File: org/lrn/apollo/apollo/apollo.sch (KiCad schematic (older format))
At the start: 53 parts, among them J1 Conn_01x01_Male, J10 Conn_01x01_Male, J11 Conn_01x01_Male, J2 Conn_01x01_Male, J3 Conn_01x01_Male, J4 Conn_01x01_Male, J5 Conn_01x01_Male, J6 Conn_01x01_Male, J7 Conn_01x01_Male, J8 Conn_01x01_Male, J9 Conn_01x01_Male, K1 SRD-05VDC-SL-C, Q1 PN2222A, Q2 PN2222A, Q3 PN2222A, Q4 PN2222A, Q5 PN2222A, U1 74HC595, U2 5461AS-1, U3 74HC595, U4 ATmega168P-20PU

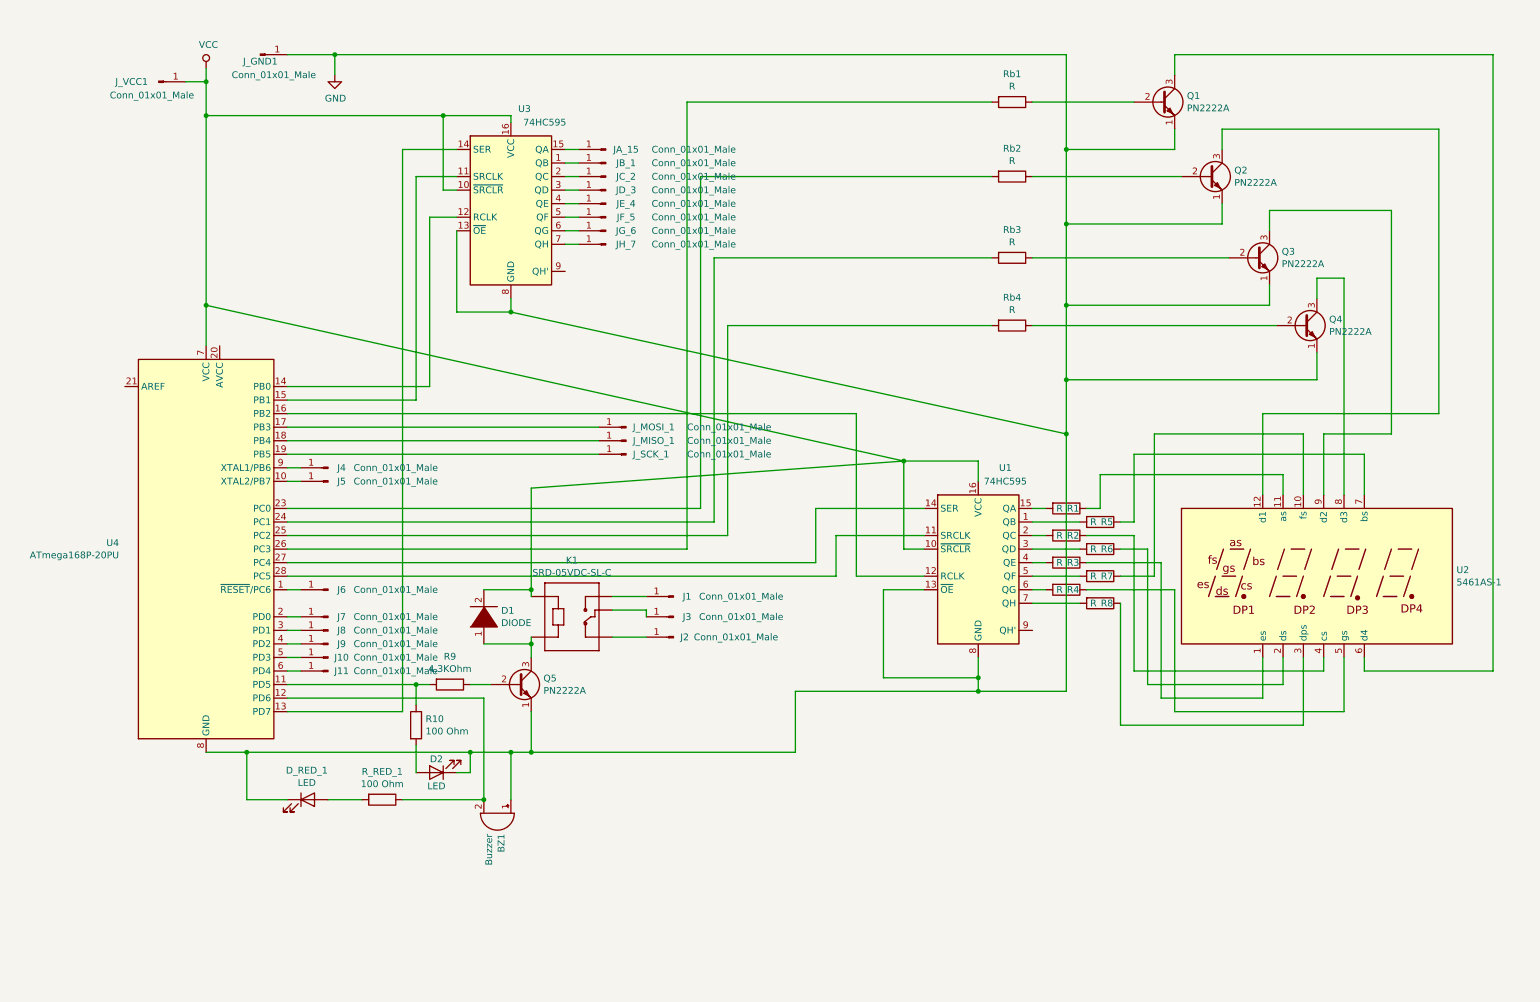
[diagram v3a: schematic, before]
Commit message: apollo: pcb improvements - separate two part of functuionality: display and control
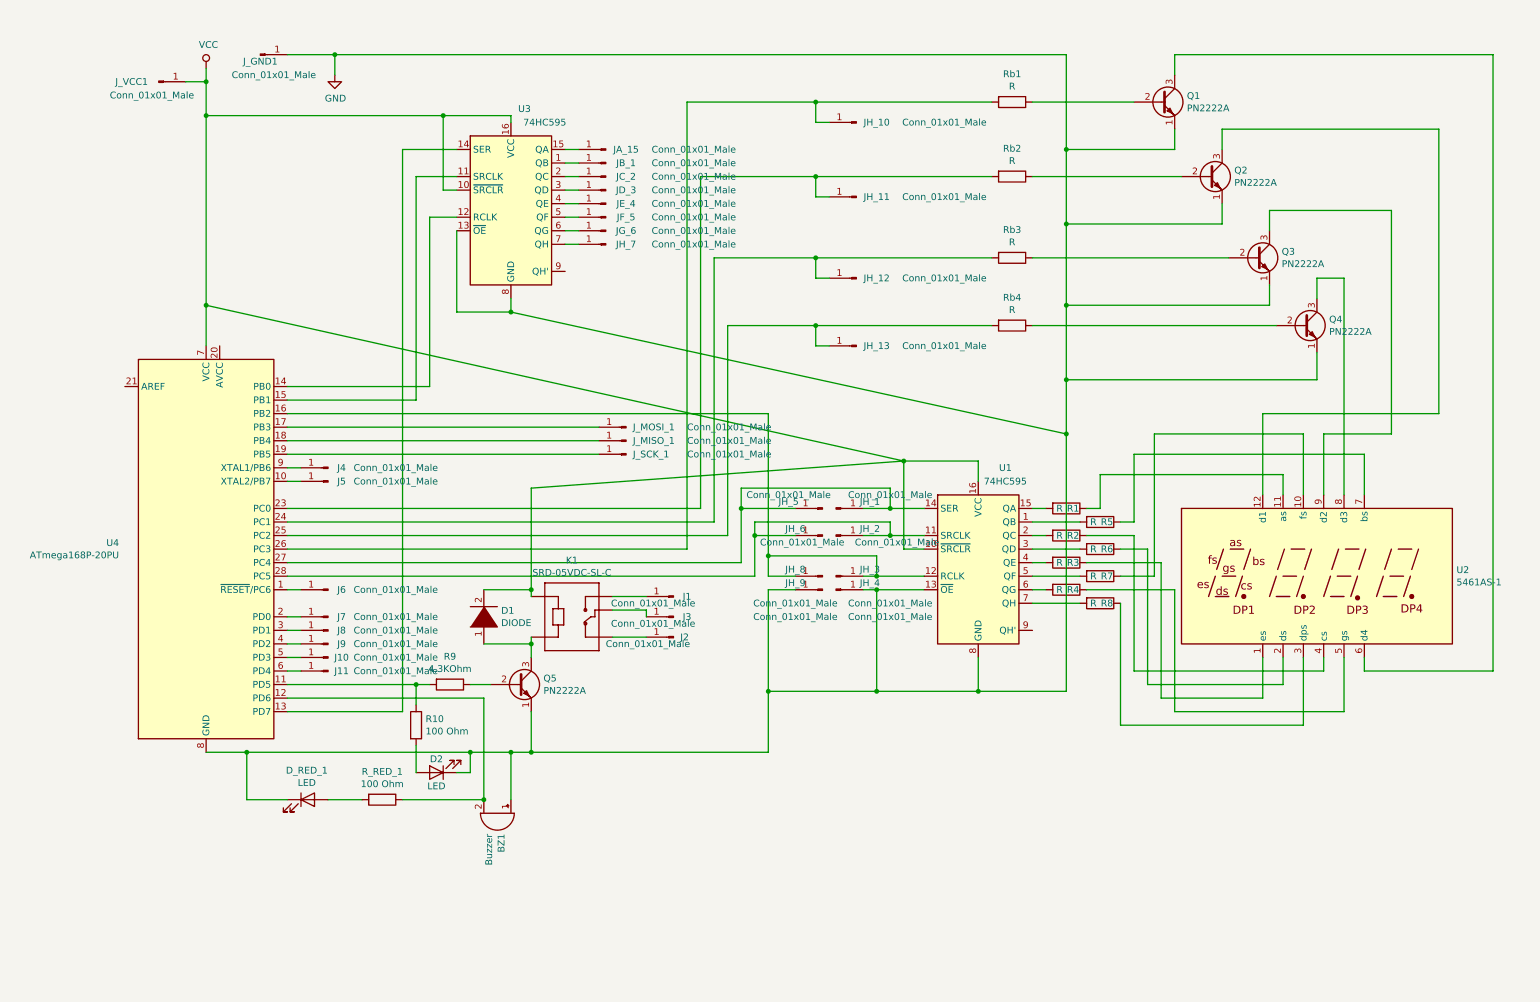
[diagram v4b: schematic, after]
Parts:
- added JH_1, JH_10, JH_11, JH_12, JH_13, JH_2, JH_3, JH_4, JH_5, JH_6, JH_8, JH_9: Conn_01x01_Male, Connector_Pin:Pin_D0.7mm_L6.5mm_W1.8mm_FlatFork, symbol Connector:Conn_01x01_Male
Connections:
- net GND: now also JH_4.1 (Pin_1), JH_9.1 (Pin_1)
- net at U1.11 (SRCLK), U4.28 (PC5): now also JH_2.1 (Pin_1), JH_6.1 (Pin_1)
- net at U1.12 (RCLK), U4.16 (PB2): now also JH_3.1 (Pin_1), JH_8.1 (Pin_1)
- net at U1.14 (SER), U4.27 (PC4): now also JH_1.1 (Pin_1), JH_5.1 (Pin_1)
- net at Rb1.2, U4.26 (PC3): now also JH_10.1 (Pin_1)
- net at Rb2.2, U4.23 (PC0): now also JH_11.1 (Pin_1)
- net at Rb3.2, U4.24 (PC1): now also JH_12.1 (Pin_1)
- net at Rb4.2, U4.25 (PC2): now also JH_13.1 (Pin_1)

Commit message: apollo: global refactoring for schematic and add relay_2
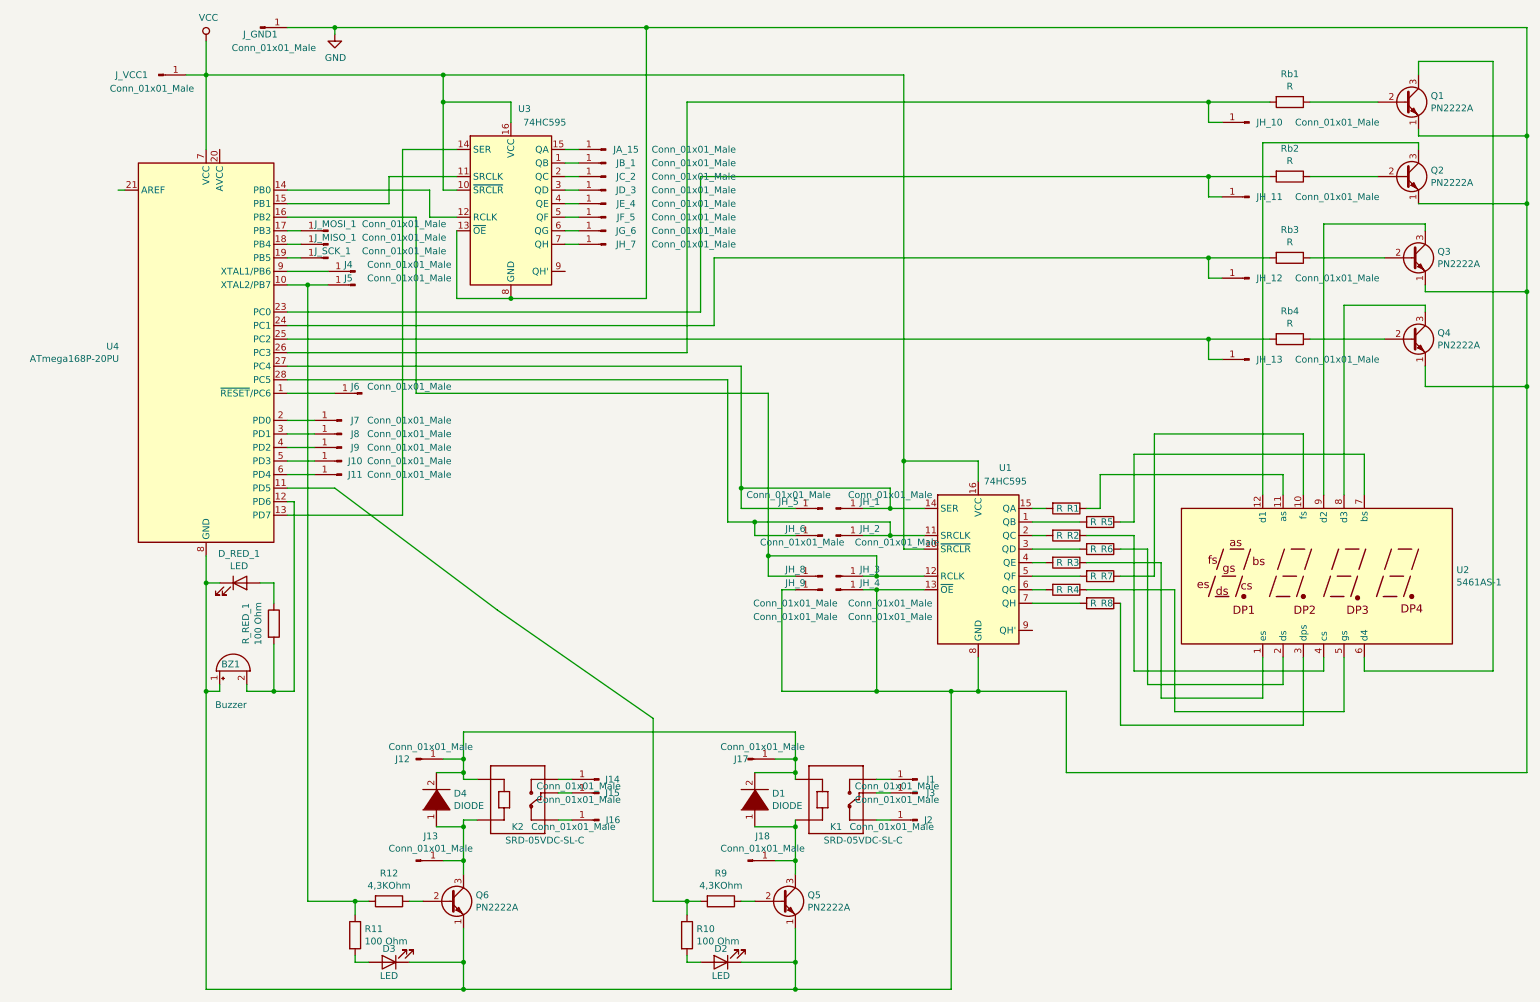
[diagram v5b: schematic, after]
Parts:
- added D3: LED, LED_THT:LED_D5.0mm_FlatTop, symbol Device:LED
- added D4: DIODE, apollo:D__Horizontal, symbol pspice:DIODE
- added J12, J13, J14, J15, J16, J17, J18: Conn_01x01_Male, Connector_Pin:Pin_D0.7mm_L6.5mm_W1.8mm_FlatFork, symbol Connector:Conn_01x01_Male
- added K2: SRD-05VDC-SL-C, apollo:RELAY_SRD-05VDC-SL-C, symbol SRD-05VDC-SL-C:SRD-05VDC-SL-C
- added Q6: PN2222A, apollo:2N222A-TO-92_Wide, symbol Transistor_BJT:PN2222A
- added R11: 100 Ohm, apollo:R__Horizontal, symbol Device:R
- added R12: 4,3KOhm, apollo:R__Horizontal, symbol Device:R
- D1: footprint apollo:R__Horizontal -> apollo:D__Horizontal
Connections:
- net GND: now also D3.1 (K), Q6.1 (E)
- net VCC: no longer D1.2 (A), K1.A1
- net at J5.1 (Pin_1), U4.10 (XTAL2/PB7): now also R11.1, R12.2
- net at BZ1.2 (+), U4.12 (PD6): now also R_RED_1.2; no longer R_RED_1.1
- net at D_RED_1.2 (A): now also R_RED_1.1; no longer R_RED_1.2
- net at D1.1 (K), K1.A2, Q5.3 (C): now also J18.1 (Pin_1)
- new net: D1.2 (A), D4.2 (A), J12.1 (Pin_1), J17.1 (Pin_1), K1.A1, K2.A1
- new net: Q6.2 (B), R12.1
- new net: D4.1 (K), J13.1 (Pin_1), K2.A2, Q6.3 (C)
- new net: J15.1 (Pin_1), K2.COM
- new net: J16.1 (Pin_1), K2.NC
- new net: J14.1 (Pin_1), K2.NO
- new net: D3.2 (A), R11.2
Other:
- moved on the sheet: BZ1, D1, D2, D_RED_1, J1, J10, J11, J2, J3, J4, J5, J6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

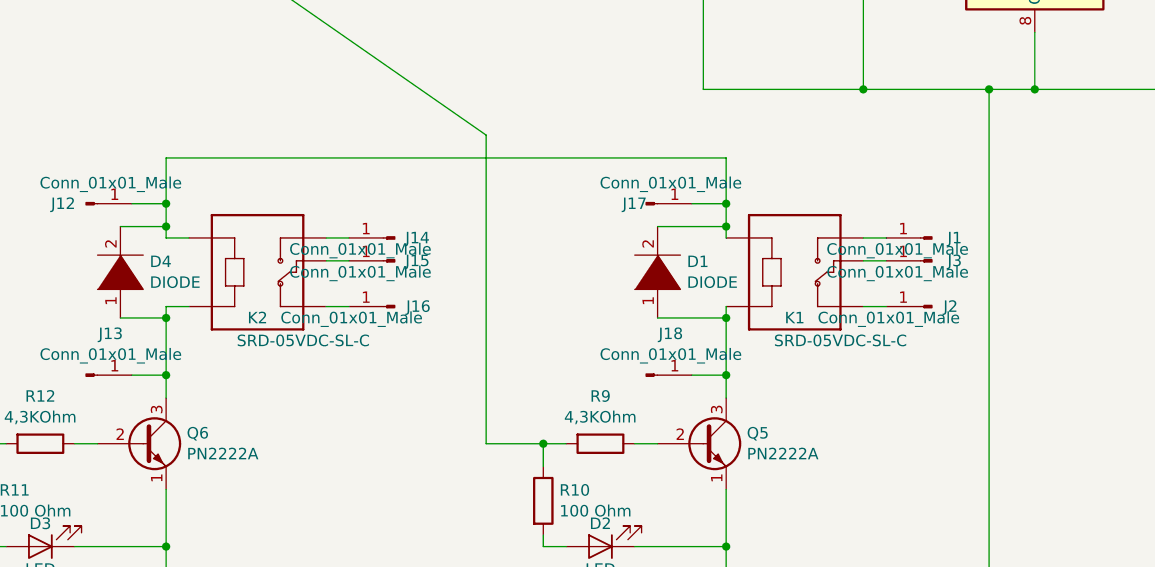
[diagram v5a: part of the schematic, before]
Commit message: apollo: remove relays (connectors instead)
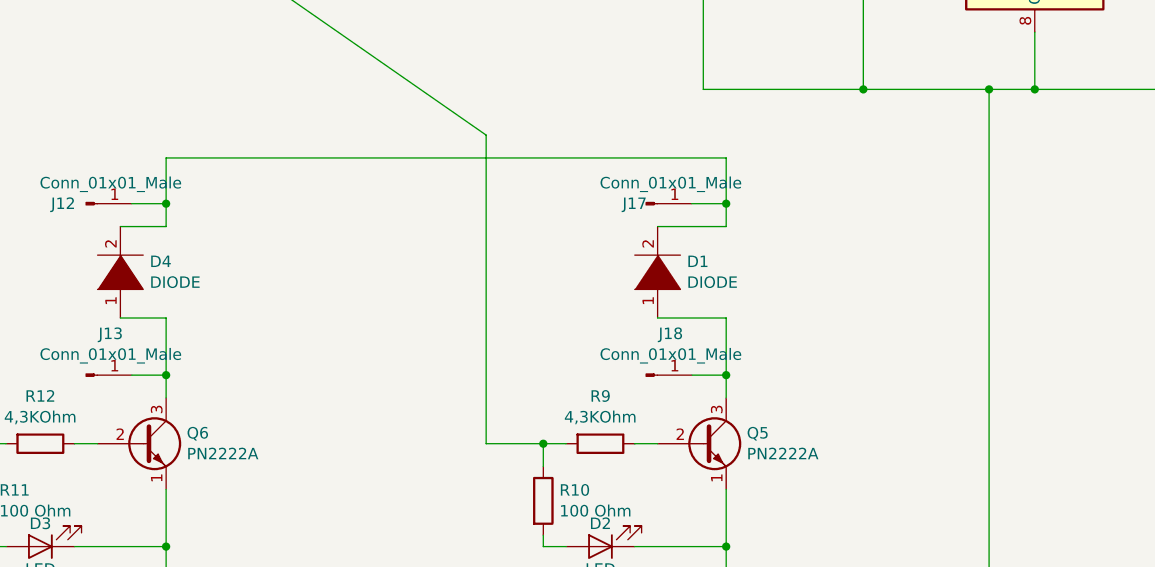
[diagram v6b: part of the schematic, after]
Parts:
- removed J1, J14, J15, J16, J2, J3: Conn_01x01_Male, Connector_Pin:Pin_D0.7mm_L6.5mm_W1.8mm_FlatFork, symbol Connector:Conn_01x01_Male
- removed K1, K2: SRD-05VDC-SL-C, apollo:RELAY_SRD-05VDC-SL-C, symbol SRD-05VDC-SL-C:SRD-05VDC-SL-C
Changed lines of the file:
@@
-$EndComp
-$Comp
-L SRD-05VDC-SL-C:SRD-05VDC-SL-C K1
-U 1 1 5F789B70
-P 6000 6250
-F 0 "K1" H 6000 6000 50  0000 C CNN
-F 1 "SRD-05VDC-SL-C" H 6200 5900 50  0000 C CNN
-F 2 "apollo:RELAY_SRD-05VDC-SL-C" H 6000 6250 50  0001 L BNN
-F 3 "IPC-7251" H 6000 6250 50  0001 L BNN
-F 4 "SONGLE RELAY" H 6000 6250 50  0001 L BNN "Field4"
-	1    6000 6250
-	1    0    0    -1
 $EndComp
 $Comp
@@
 $EndComp
 $Comp
-L Connector:Conn_01x01_Male J2
-U 1 1 5F7F3157
-P 6600 6450
-F 0 "J2" H 6550 6450 50  0000 R CNN
-F 1 "Conn_01x01_Male" H 7100 6500 50  0000 R CNN
-F 2 "Connector_Pin:Pin_D0.7mm_L6.5mm_W1.8mm_FlatFork" H 6600 6450 50  0001 C CNN
-F 3 "~" H 6600 6450 50  0001 C CNN
-	1    6600 6450
-	-1   0    0    1
-$EndComp
-$Comp
-L Connector:Conn_01x01_Male J1
-U 1 1 5F7F3A36
-P 6600 6150
-F 0 "J1" H 6500 6150 50  0000 C CNN
-F 1 "Conn_01x01_Male" H 6750 6200 50  0000 C CNN
-F 2 "Connector_Pin:Pin_D0.7mm_L6.5mm_W1.8mm_FlatFork" H 6600 6150 50  0001 C CNN
-F 3 "~" H 6600 6150 50  0001 C CNN
-	1    6600 6150
-	-1   0    0    1
-$EndComp
-$Comp
 L Device:R R10
 U 1 1 5F73C2C8
@@
 F 3 "~" H 5150 7500 50  0001 C CNN
 	1    5150 7500
-	-1   0    0    1
-$EndComp
-$Comp
-L Connector:Conn_01x01_Male J3
-U 1 1 5F74C3F1
-P 6600 6250
-F 0 "J3" H 6500 6250 50  0000 C CNN
-F 1 "Conn_01x01_Male" H 6750 6300 50  0000 C CNN
-F 2 "Connector_Pin:Pin_D0.7mm_L6.5mm_W1.8mm_FlatFork" H 6600 6250 50  0001 C CNN
-F 3 "~" H 6600 6250 50  0001 C CNN
-	1    6600 6250
 	-1   0    0    1
 $EndComp
@@
 $EndComp
 $Comp
-L Connector:Conn_01x01_Male J16
-U 1 1 5F8BDA7E
-P 4250 6450
-F 0 "J16" H 4200 6450 50  0000 R CNN
-F 1 "Conn_01x01_Male" H 4750 6500 50  0000 R CNN
-F 2 "Connector_Pin:Pin_D0.7mm_L6.5mm_W1.8mm_FlatFork" H 4250 6450 50  0001 C CNN
-F 3 "~" H 4250 6450 50  0001 C CNN
-	1    4250 6450
-	-1   0    0    1
-$EndComp
-$Comp
-L Connector:Conn_01x01_Male J15
-U 1 1 5F8BDAA0
-P 4250 6250
-F 0 "J15" H 4150 6250 50  0000 C CNN
-F 1 "Conn_01x01_Male" H 4400 6300 50  0000 C CNN
-F 2 "Connector_Pin:Pin_D0.7mm_L6.5mm_W1.8mm_FlatFork" H 4250 6250 50  0001 C CNN
-F 3 "~" H 4250 6250 50  0001 C CNN
-	1    4250 6250
-	-1   0    0    1
-$EndComp
-$Comp
-L Connector:Conn_01x01_Male J14
-U 1 1 5F8BDA84
-P 4250 6150
-F 0 "J14" H 4150 6150 50  0000 C CNN
-F 1 "Conn_01x01_Male" H 4400 6200 50  0000 C CNN
-F 2 "Connector_Pin:Pin_D0.7mm_L6.5mm_W1.8mm_FlatFork" H 4250 6150 50  0001 C CNN
-F 3 "~" H 4250 6150 50  0001 C CNN
-	1    4250 6150
-	-1   0    0    1
-$EndComp
-$Comp
 L pspice:DIODE D4
 U 1 1 5F8BDA73
@@
 	1    0    0    -1
 $EndComp
-$Comp
-L SRD-05VDC-SL-C:SRD-05VDC-SL-C K2
-U 1 1 5F8BDA6D
-P 3650 6250
-F 0 "K2" H 3650 6000 50  0000 C CNN
-F 1 "SRD-05VDC-SL-C" H 3850 5900 50  0000 C CNN
-F 2 "apollo:RELAY_SRD-05VDC-SL-C" H 3650 6250 50  0001 L BNN
-F 3 "IPC-7251" H 3650 6250 50  0001 L BNN
-F 4 "SONGLE RELAY" H 3650 6250 50  0001 L BNN "Field4"
-	1    3650 6250
-	1    0    0    -1
-$EndComp
 Wire Wire Line
 	3100 6000 3250 6000
 Wire Wire Line
-	3250 6150 3350 6150
-Wire Wire Line
 	3100 6750 3250 6750
-Wire Wire Line
-	3250 6450 3350 6450
 Wire Wire Line
 	3250 6750 3250 6850
@@
 	5550 6750 5700 6750
 Wire Wire Line
-	3950 6150 4050 6150
-Wire Wire Line
-	3950 6250 4050 6250
-Wire Wire Line
-	3950 6450 4050 6450
-Wire Wire Line
-	6300 6150 6400 6150
-Wire Wire Line
-	6300 6250 6400 6250
-Wire Wire Line
-	6300 6450 6400 6450
-Wire Wire Line
 	3250 6000 3250 6100
 Wire Wire Line
-	3250 6450 3250 6500
-Wire Wire Line
 	3050 6100 3250 6100
-Connection ~ 3250 6100
-Wire Wire Line
-	3250 6100 3250 6150
 Wire Wire Line
 	3050 6500 3250 6500
-Connection ~ 3250 6500
 Wire Wire Line
 	3250 6500 3250 6750
@@
 	5700 6000 5700 6100
 Wire Wire Line
-	5700 6450 5700 6500
-Wire Wire Line
 	5400 6100 5700 6100
-Connection ~ 5700 6100
-Wire Wire Line
-	5700 6100 5700 6150
 Wire Wire Line
 	5400 6500 5700 6500
-Connection ~ 5700 6500
 Wire Wire Line
 	5700 6500 5700 6750

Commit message: apollo:pcb improvement
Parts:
- removed J5: Conn_01x01_Male, Connector_Pin:Pin_D0.7mm_L6.5mm_W1.8mm_FlatFork, symbol Connector:Conn_01x01_Male
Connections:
- net VCC: now also D1.2 (A), D4.2 (A), J12.1 (Pin_1), J17.1 (Pin_1), JA_15.1 (Pin_1), JB_1.1 (Pin_1), JC_2.1 (Pin_1), JD_3.1 (Pin_1), JE_4.1 (Pin_1), JF_5.1 (Pin_1), JG_6.1 (Pin_1), JH_7.1 (Pin_1), U3.1 (QB), U3.15 (QA), U3.2 (QC), U3.3 (QD), U3.4 (QE), U3.5 (QF), U3.6 (QG), U3.7 (QH)
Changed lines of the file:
@@
-$EndComp
-$Comp
-L Connector:Conn_01x01_Male J5
-U 1 1 5F78ED5D
-P 2450 2500
-F 0 "J5" H 2500 2450 50  0000 C CNN
-F 1 "Conn_01x01_Male" H 2050 2450 50  0000 C CNN
-F 2 "Connector_Pin:Pin_D0.7mm_L6.5mm_W1.8mm_FlatFork" H 2450 2500 50  0001 C CNN
-F 3 "~" H 2450 2500 50  0001 C CNN
-	1    2450 2500
-	-1   0    0    1
 $EndComp
 $Comp
@@
 Connection ~ 6850 5500
 Wire Wire Line
-	3250 5800 5700 5800
-Wire Wire Line
-	3100 950  6500 950
+	3250 5800 4100 5800
+Wire Wire Line
+	3100 950  4100 950
 Connection ~ 2450 7050
 Wire Wire Line
@@
 Wire Wire Line
 	2100 7050 2450 7050
-Connection ~ 2100 2500
-Wire Wire Line
-	2100 2500 2250 2500
 Wire Wire Line
 	1950 3300 2300 3300
@@
 Wire Wire Line
 	5700 7700 6850 7700
+Wire Wire Line
+	4100 950  4100 1500
+Connection ~ 4100 950
+Wire Wire Line
+	4100 950  6500 950
+Connection ~ 4100 5800
+Wire Wire Line
+	4100 5800 5700 5800
+Connection ~ 4100 1500
+Wire Wire Line
+	4100 1500 4100 1600
+Connection ~ 4100 1600
+Wire Wire Line
+	4100 1600 4100 1700
+Connection ~ 4100 1700
+Wire Wire Line
+	4100 1700 4100 1800
+Connection ~ 4100 1800
+Wire Wire Line
+	4100 1800 4100 1900
+Connection ~ 4100 1900
+Wire Wire Line
+	4100 1900 4100 2000
+Connection ~ 4100 2000
+Wire Wire Line
+	4100 2000 4100 2100
+Connection ~ 4100 2100
+Wire Wire Line
+	4100 2100 4100 2200
+Connection ~ 4100 2200
+Wire Wire Line
+	4100 2200 4100 5800
 $EndSCHEMATC
